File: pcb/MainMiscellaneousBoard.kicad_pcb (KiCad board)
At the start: 2 copper layers, 66 x 70 mm, 2 parts

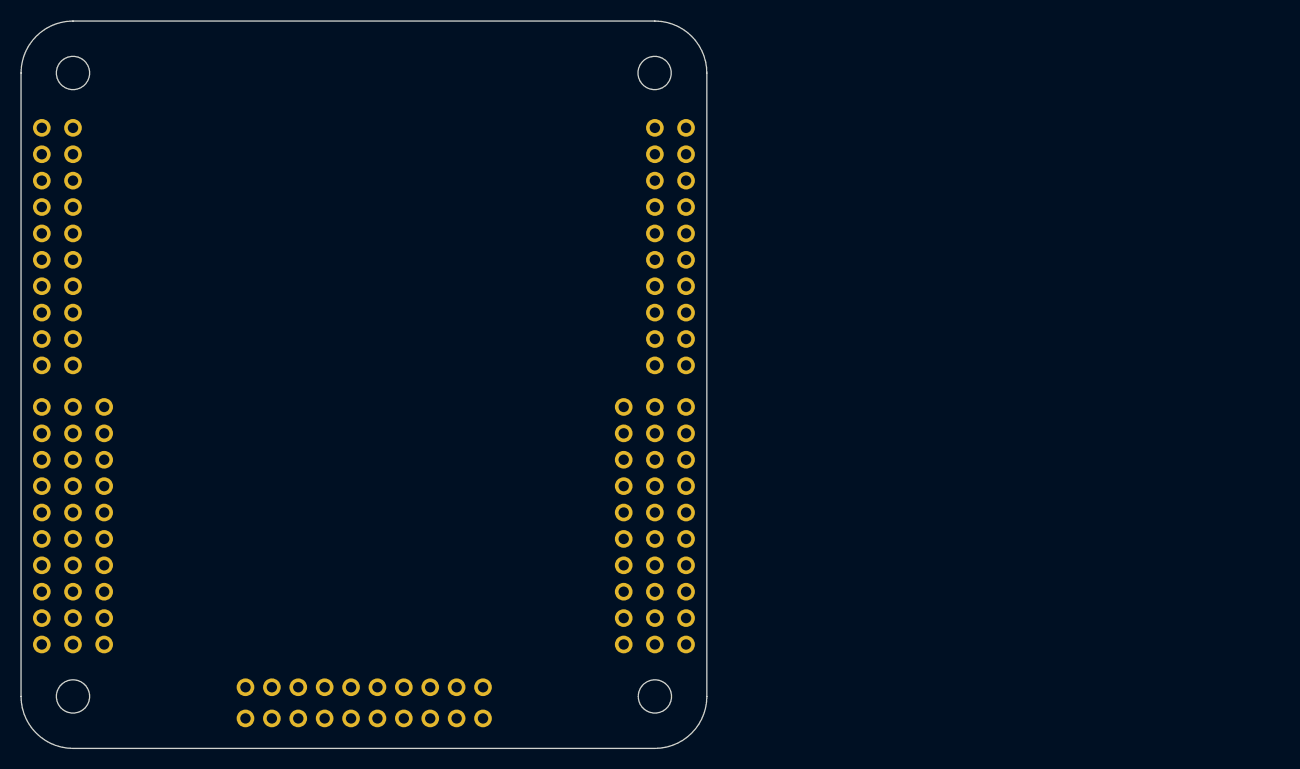
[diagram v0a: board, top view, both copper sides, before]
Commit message: Updated main miscellaneous board with new stack-up layout.
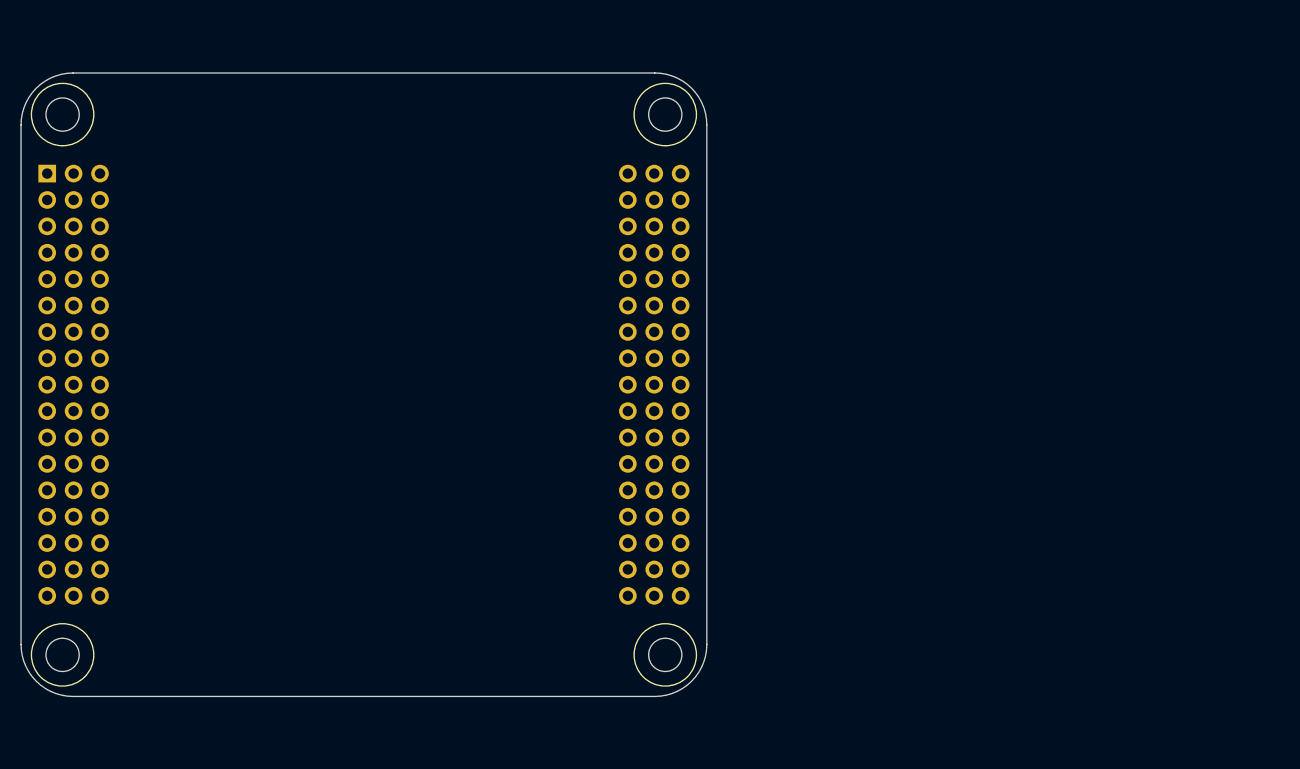
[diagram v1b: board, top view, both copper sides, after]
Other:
- board size 66 x 70 mm -> 66 x 60 mm

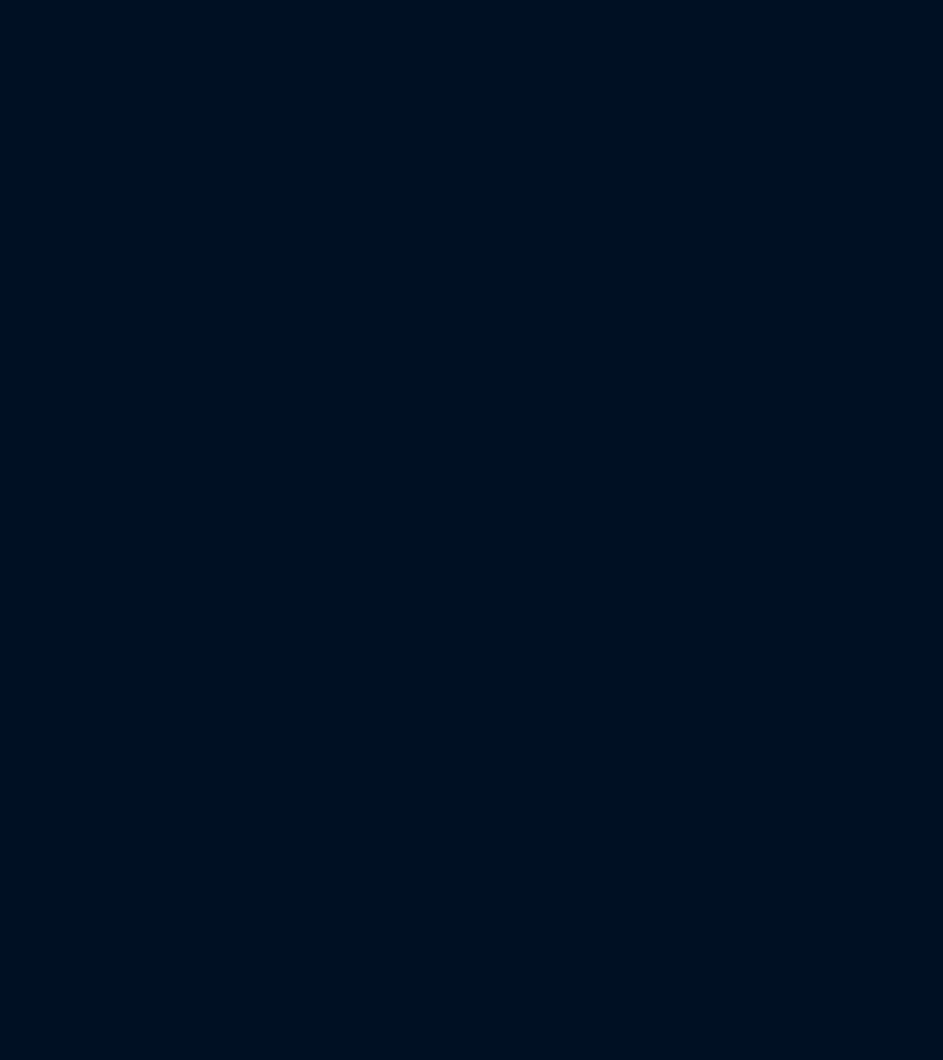
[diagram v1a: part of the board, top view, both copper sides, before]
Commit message: uSD Connector (V6 : Hierarchical labels).
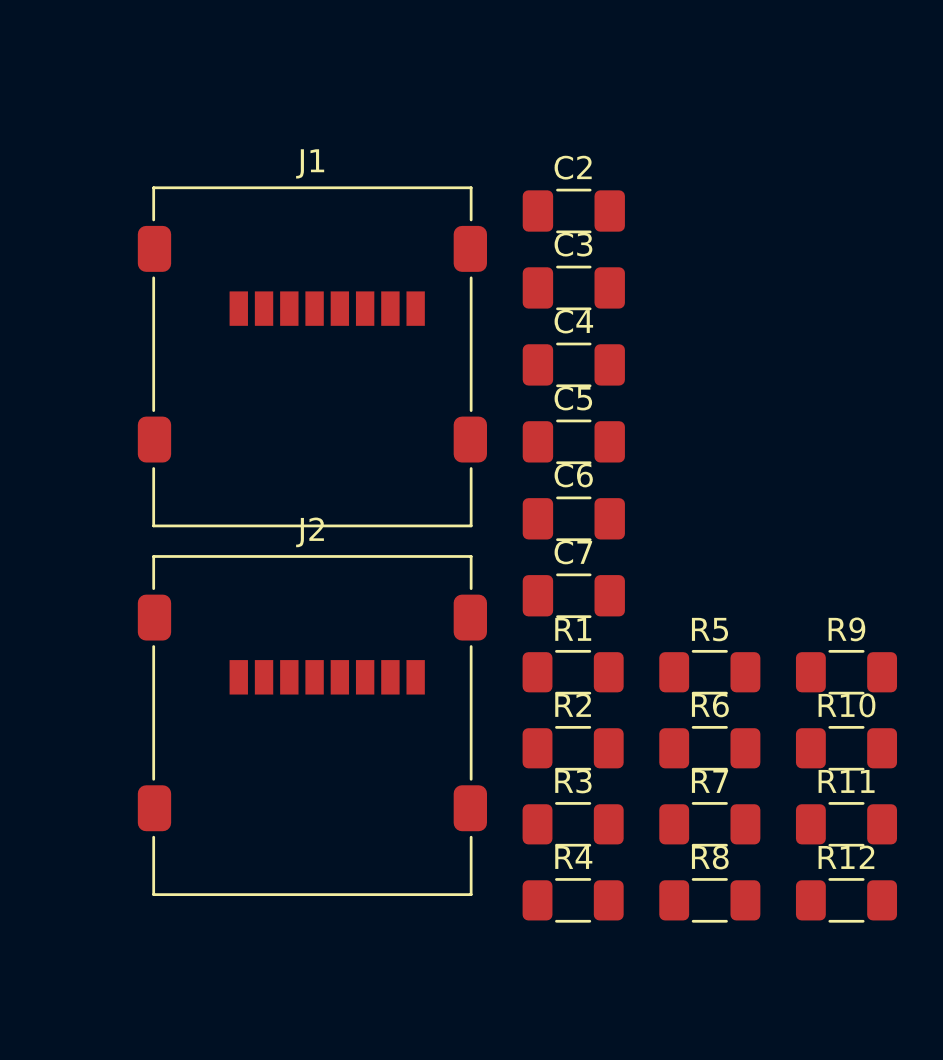
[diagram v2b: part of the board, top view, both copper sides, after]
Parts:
- added C2: 1u, Capacitor_SMD:C_1206_3216Metric_Pad1.33x1.80mm_HandSolder, F.Cu at (224.0, 94.0)
- added C3: 100n, Capacitor_SMD:C_1206_3216Metric_Pad1.33x1.80mm_HandSolder, F.Cu at (224.0, 97.3)
- added C4: 10n, Capacitor_SMD:C_1206_3216Metric_Pad1.33x1.80mm_HandSolder, F.Cu at (224.0, 100.7)
- added C5: 1u, Capacitor_SMD:C_1206_3216Metric_Pad1.33x1.80mm_HandSolder, F.Cu at (224.0, 104.0)
- added C6: 100n, Capacitor_SMD:C_1206_3216Metric_Pad1.33x1.80mm_HandSolder, F.Cu at (224.0, 107.4)
- added C7: 10n, Capacitor_SMD:C_1206_3216Metric_Pad1.33x1.80mm_HandSolder, F.Cu at (224.0, 110.7)
- added J1: 0472192001, pcb:microSD_HC_Molex_47219-2001, F.Cu at (212.6, 100.3)
- added J2: 0472192001, pcb:microSD_HC_Molex_47219-2001, F.Cu at (212.6, 116.4)
- added R1: R_Small, Resistor_SMD:R_1206_3216Metric_Pad1.30x1.75mm_HandSolder, F.Cu at (223.9, 114.1)
- added R10: R_Small, Resistor_SMD:R_1206_3216Metric_Pad1.30x1.75mm_HandSolder, F.Cu at (235.8, 117.4)
- added R11: R_Small, Resistor_SMD:R_1206_3216Metric_Pad1.30x1.75mm_HandSolder, F.Cu at (235.8, 120.7)
- added R12: R_Small, Resistor_SMD:R_1206_3216Metric_Pad1.30x1.75mm_HandSolder, F.Cu at (235.8, 124.0)
- added R2: R_Small, Resistor_SMD:R_1206_3216Metric_Pad1.30x1.75mm_HandSolder, F.Cu at (223.9, 117.4)
- added R3: R_Small, Resistor_SMD:R_1206_3216Metric_Pad1.30x1.75mm_HandSolder, F.Cu at (223.9, 120.7)
- added R4: R_Small, Resistor_SMD:R_1206_3216Metric_Pad1.30x1.75mm_HandSolder, F.Cu at (223.9, 124.0)
- added R5: R_Small, Resistor_SMD:R_1206_3216Metric_Pad1.30x1.75mm_HandSolder, F.Cu at (229.9, 114.1)
- added R6: R_Small, Resistor_SMD:R_1206_3216Metric_Pad1.30x1.75mm_HandSolder, F.Cu at (229.9, 117.4)
- added R7: R_Small, Resistor_SMD:R_1206_3216Metric_Pad1.30x1.75mm_HandSolder, F.Cu at (229.9, 120.7)
- added R8: R_Small, Resistor_SMD:R_1206_3216Metric_Pad1.30x1.75mm_HandSolder, F.Cu at (229.9, 124.0)
- added R9: R_Small, Resistor_SMD:R_1206_3216Metric_Pad1.30x1.75mm_HandSolder, F.Cu at (235.8, 114.1)

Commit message: Added uSD card connectors for camera subsystem A and B.
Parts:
- moved J2 78.3 mm to (134.4, 119.2)
- moved J1 64.8 mm to (150.6, 119.2)
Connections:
- net XYZ_data_1 renamed camera_A_sd_cmd
- net XYZ_sd_clock renamed camera_A_sd_clock
- net XYZ_sd_cmd renamed camera_A_sd_data_1
- net XYZ_sd_data_0 renamed camera_A_sd_data_3
- net XYZ_sd_data_2 renamed camera_A_sd_data_2
- net XYZ_sd_data_3 renamed camera_A_sd_data_0
- J1 pad 1: /SD_CONNECTOR_DAT2 -> Net-(J1-DAT2)
- J1 pad 2: /SD_CONNECTOR_DAT3 -> Net-(J1-DAT3/CD)
- J1 pad 3: /SD_CONNECTOR_CMD -> Net-(J1-CMD)
- J1 pad 5: /SD_CONNECTOR_CLK -> Net-(J1-CLK)
- J1 pad 7: /SD_CONNECTOR_DAT0 -> Net-(J1-DAT0)
- J1 pad 8: /SD_CONNECTOR_DAT1 -> Net-(J1-DAT1)
- J2 pad 1: /SD_CONNECTOR_DAT2 -> Net-(J2-DAT2)
- J2 pad 2: /SD_CONNECTOR_DAT3 -> Net-(J2-DAT3/CD)
- J2 pad 3: /SD_CONNECTOR_CMD -> Net-(J2-CMD)
- J2 pad 5: /SD_CONNECTOR_CLK -> Net-(J2-CLK)
- J2 pad 7: /SD_CONNECTOR_DAT0 -> Net-(J2-DAT0)
- J2 pad 8: /SD_CONNECTOR_DAT1 -> Net-(J2-DAT1)
- R1 pad 2: /SD_CONNECTOR_DAT2 -> Net-(J1-DAT2)
- R10 pad 1: unconnected-(R10-Pad1) -> camera_B_sd_data_0
- R10 pad 2: /SD_CONNECTOR_DAT0 -> Net-(J2-DAT0)
- R11 pad 1: unconnected-(R11-Pad1) -> camera_B_sd_cmd
- R11 pad 2: /SD_CONNECTOR_CMD -> Net-(J2-CMD)
- R12 pad 1: unconnected-(R12-Pad1) -> camera_B_sd_data_1
- R12 pad 2: /SD_CONNECTOR_DAT1 -> Net-(J2-DAT1)
- R2 pad 2: /SD_CONNECTOR_CLK -> Net-(J1-CLK)
- R3 pad 2: /SD_CONNECTOR_DAT0 -> Net-(J1-DAT3/CD)
- R4 pad 2: /SD_CONNECTOR_DAT3 -> Net-(J1-DAT0)
- R5 pad 2: /SD_CONNECTOR_DAT1 -> Net-(J1-CMD)
- R6 pad 2: /SD_CONNECTOR_CMD -> Net-(J1-DAT1)
- R7 pad 1: unconnected-(R7-Pad1) -> camera_B_sd_data_2
- R7 pad 2: /SD_CONNECTOR_DAT2 -> Net-(J2-DAT2)
- R8 pad 1: unconnected-(R8-Pad1) -> camera_B_sd_clock
- R8 pad 2: /SD_CONNECTOR_CLK -> Net-(J2-CLK)
- R9 pad 1: unconnected-(R9-Pad1) -> camera_B_sd_data_3
- R9 pad 2: /SD_CONNECTOR_DAT3 -> Net-(J2-DAT3/CD)

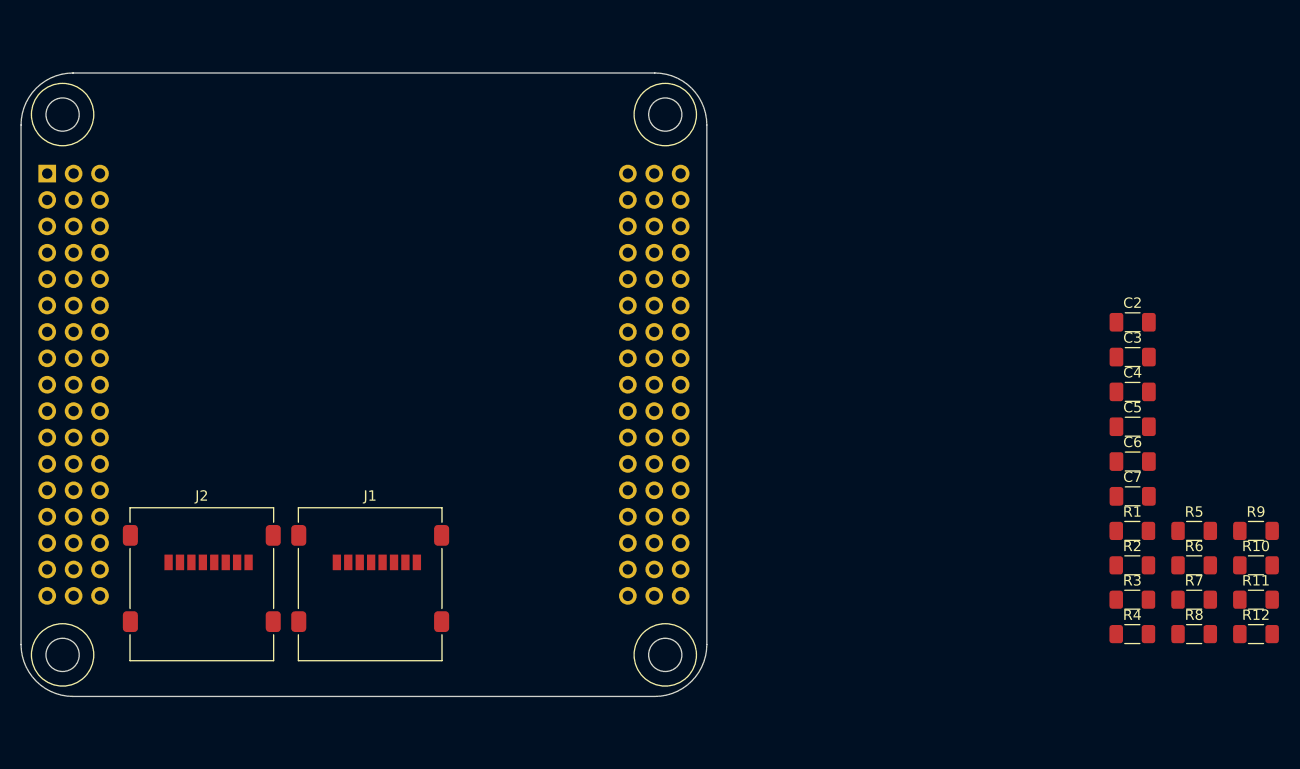
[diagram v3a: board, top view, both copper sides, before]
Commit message: Made symbol for ItsyBitsy ESP32.
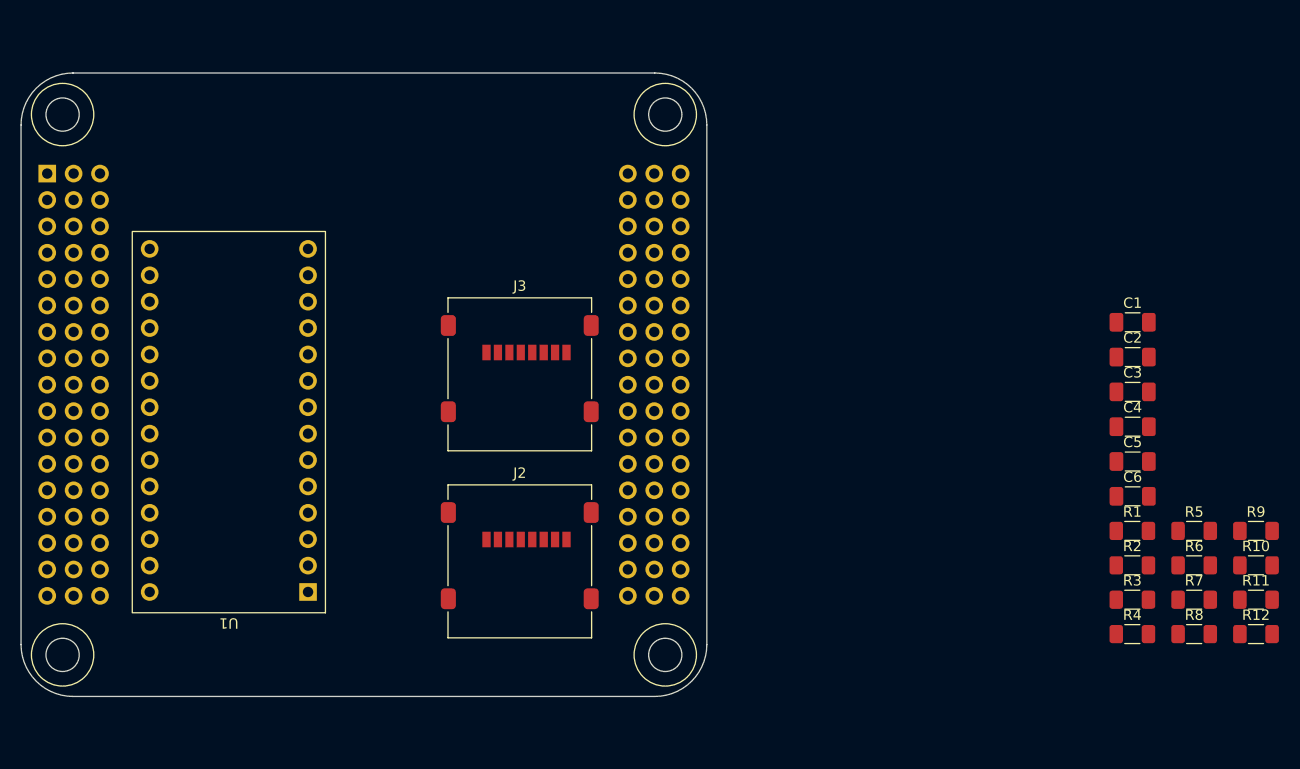
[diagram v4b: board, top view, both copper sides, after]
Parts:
- added U1: ItsyBitsy_ESP32, pcb:ItsyBitsy_ESP32, F.Cu at (144.6, 119.9)
- C1: renamed from C2; value 1u -> C_Small
- C2: renamed from C3; value 100n -> C_Small
- C3: renamed from C4; value 10n -> C_Small
- C4: renamed from C5; value 1u -> C_Small
- C5: renamed from C6; value 100n -> C_Small
- C6: renamed from C7; value 10n -> C_Small
- J2: renamed from J1; value 0472192001 -> Micro_SD_Card
- J3: renamed from J2; value 0472192001 -> Micro_SD_Card
- moved J3 36.7 mm to (165.0, 99.0)
- moved J2 14.6 mm to (165.0, 117.0)
- renumbered C1 to J1

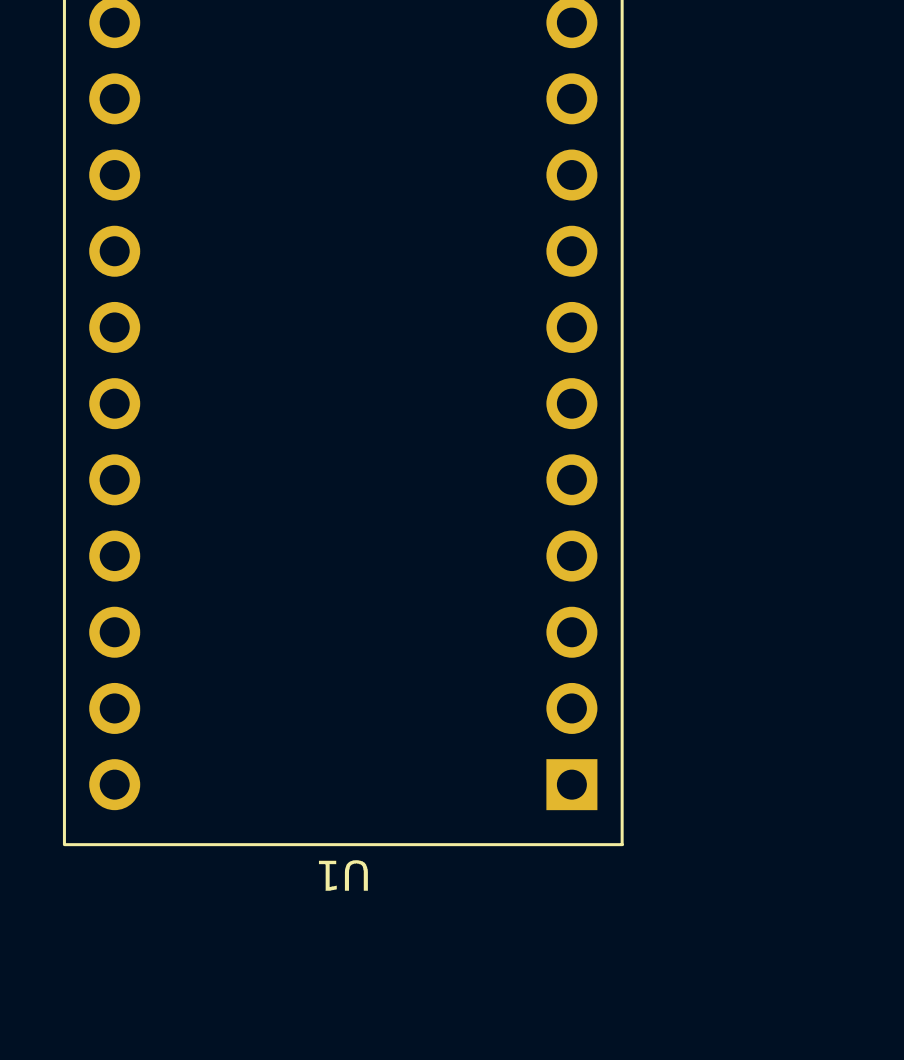
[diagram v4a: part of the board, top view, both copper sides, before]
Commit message: Made SEEED Studio XIAO ESP32-S3 Sense symbol and footprint.
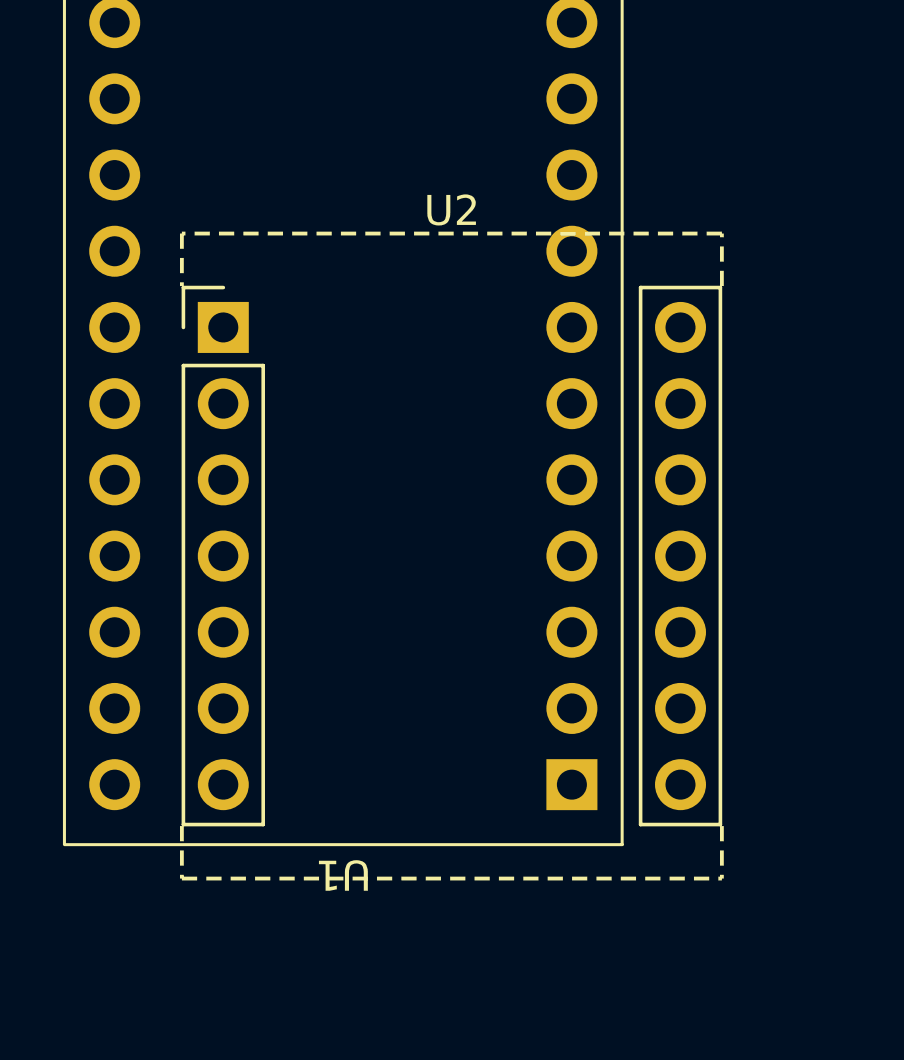
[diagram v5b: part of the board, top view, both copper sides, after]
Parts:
- added U2: Seeed_Studio_XIAO-ESP32-S3-Sense, pcb:Seeed_Studio_XIAO_ESP32_S3, F.Cu at (140.6, 112.3)
